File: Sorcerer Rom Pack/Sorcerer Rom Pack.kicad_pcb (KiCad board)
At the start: 2 copper layers, 119.4 x 73.3 mm, 86 parts, among them J1 ROMRD15, J10 A11, J11 A13, J12 A12, J13 A, J14 A, J15 A, J16 A, J17 A, J18 C, J19 B, J2 A14, J20 A, J21 A, J22 A, J23 A, J24 A, J25 A, J26 A, J27 A, J28 Sorcerer Cart Slot, J29 0 ENABLE, J3 ROMRD15, J30 1 ENABLE, J31 4 ENABLE, J32 5 ENABLE, J33 1 PROM, J34 2 PROM, J35 A, J36 A, J37 A, J38 A, J39 A, J4 A12, J40 A, J41 A, J42 A, J43 A, J44 A, J45 A, J46 A, J47 A, J48 A, J49 A, J5 Conn_01x01, J50 A, J51 A, J52 A, J53 A, J54 A, J55 A, J56 A, J57 A, J58 A, J59 A, J6 Conn_01x01, J60 A, J61 A, J62 A, J63 A, J64 A, J65 A, J66 A, J67 A, J68 A, J69 RAM cut, J7 A, J8 A14, J9 A10, U1 2716, U2 2716, U3 2716, U4 2716, U5 74LS11, U6 74LS138

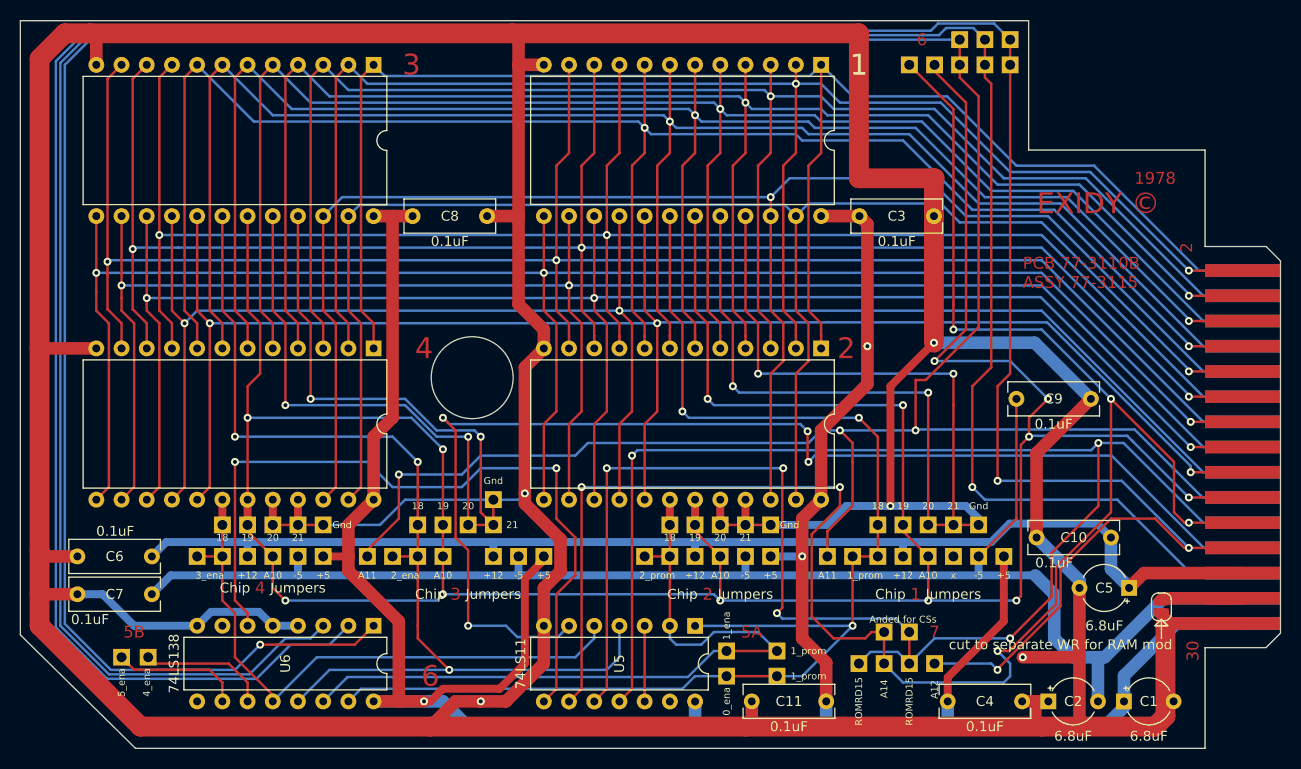
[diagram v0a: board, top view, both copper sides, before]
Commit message: many tweaks and experimental silk
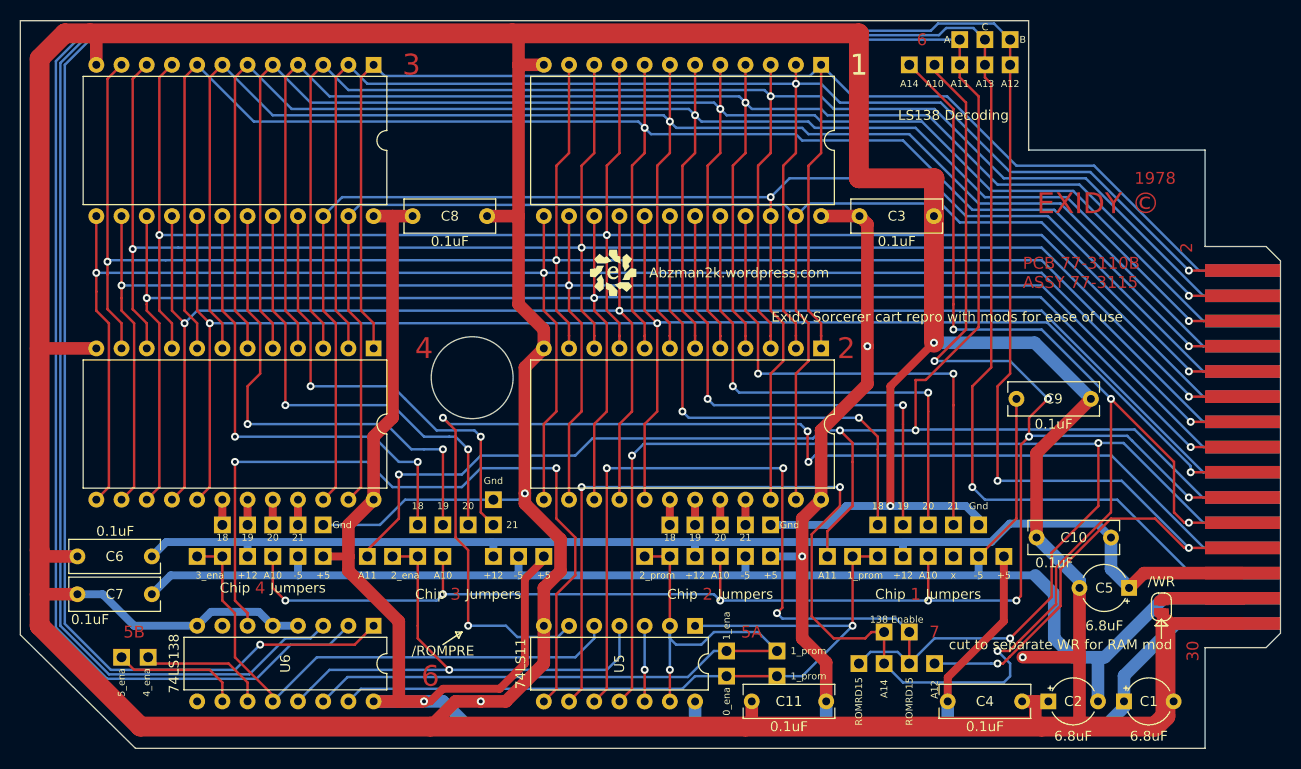
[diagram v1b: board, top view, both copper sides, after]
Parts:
- added G***: LOGO, Evan's misc parts:Evan Logo, F.Cu at (129.5, 95.9)
- added G***: LOGO, Evan's misc parts:OSHW gear, B.Cu at (183.5, 107.3)
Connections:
- J16 pad 1: 30 -> Net-(J16-Pad1)
- J21 pad 1: 30 -> Net-(J21-Pad1)
- J23 pad 1: 20 -> Net-(J23-Pad1)
- J25 pad 1: Net-(J24-Pad1) -> Net-(J25-Pad1)
- J30 pad 1: Net-(J34-Pad1) -> Net-(J30-Pad1)
- J34 pad 1: Net-(J34-Pad1) -> Net-(J30-Pad1)
- J38 pad 1: 30 -> Net-(J38-Pad1)
- J40 pad 1: 30 -> Net-(J40-Pad1)
- J42 pad 1: 20 -> Net-(J42-Pad1)
- J43 pad 1: Net-(J34-Pad1) -> Net-(J30-Pad1)
- J44 pad 1: Net-(J34-Pad1) -> Net-(J44-Pad1)
- J45 pad 1: Net-(J34-Pad1) -> Net-(J30-Pad1)
- J49 pad 1: 30 -> Net-(J49-Pad1)
- J51 pad 1: 30 -> Net-(J51-Pad1)
- J53 pad 1: 20 -> Net-(J53-Pad1)
- J55 pad 1: Net-(J54-Pad1) -> Net-(J55-Pad1)
- J61 pad 1: 30 -> Net-(J61-Pad1)
- J63 pad 1: 30 -> Net-(J63-Pad1)
- J65 pad 1: 20 -> Net-(J65-Pad1)
- J67 pad 1: Net-(J66-Pad1) -> Net-(J67-Pad1)
- U1 pad 18: Net-(J24-Pad1) -> Net-(J25-Pad1)
- U1 pad 19: 20 -> Net-(J23-Pad1)
- U1 pad 20: 30 -> Net-(J21-Pad1)
- U1 pad 21: 30 -> Net-(J16-Pad1)
- U2 pad 18: Net-(J34-Pad1) -> Net-(J44-Pad1)
- U2 pad 19: 20 -> Net-(J42-Pad1)
- U2 pad 20: 30 -> Net-(J40-Pad1)
- U2 pad 21: 30 -> Net-(J38-Pad1)
- U3 pad 18: Net-(J54-Pad1) -> Net-(J55-Pad1)
- U3 pad 19: 20 -> Net-(J53-Pad1)
- U3 pad 20: 30 -> Net-(J51-Pad1)
- U3 pad 21: 30 -> Net-(J49-Pad1)
- U4 pad 18: Net-(J66-Pad1) -> Net-(J67-Pad1)
- U4 pad 19: 20 -> Net-(J65-Pad1)
- U4 pad 20: 30 -> Net-(J63-Pad1)
- U4 pad 21: 30 -> Net-(J61-Pad1)
- U5 pad 13: Net-(J34-Pad1) -> Net-(J30-Pad1)
- U5 pad 2: Net-(J34-Pad1) -> Net-(J30-Pad1)
- U6 pad 14: Net-(J34-Pad1) -> Net-(J30-Pad1)
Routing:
- net 30: track 804.7 -> 576.6 mm, vias 13 -> 5
- net 20: track 313.3 -> 183.1 mm, vias 13 -> 9
- net Net-(J30-Pad1): track 0.00 -> 78.6 mm, vias 0 -> 1
- net Net-(J34-Pad1): track 76.7 -> 0.00 mm
- net Net-(J24-Pad1): track 132.4 -> 79.4 mm, vias 3 -> 1
- net Net-(J54-Pad1): track 104.4 -> 52.7 mm, vias 3 -> 1
- net Net-(J16-Pad1): track 0.00 -> 51.3 mm, vias 0 -> 2
- net Net-(J23-Pad1): track 0.00 -> 51.0 mm, vias 0 -> 2
- net Net-(J21-Pad1): track 0.00 -> 51.0 mm, vias 0 -> 2
- net Net-(J53-Pad1): track 0.00 -> 50.4 mm, vias 0 -> 2
- net Net-(J25-Pad1): track 0.00 -> 49.8 mm, vias 0 -> 2
- net Net-(J55-Pad1): track 0.00 -> 48.6 mm, vias 0 -> 2
- net Net-(J51-Pad1): track 0.00 -> 47.5 mm, vias 0 -> 2
- net Net-(J49-Pad1): track 0.00 -> 46.3 mm, vias 0 -> 2
- net Net-(J66-Pad1): track 61.2 -> 55.5 mm
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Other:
- board text added: "/ROMPRE"
- board text added: "/WR"
- board text added: "138 Enable"
- board text added: "138 Enable jumpers set the starting address A14/ROMRD15 = C000 (use for 8K PAC) A13/ROMRD15 = A000 (use for 16K PAC) A12/ROMRD15 = 9000 ROMRD15 x2 = 8000"
- board text added: "16K ROM PAC 4K ROMS A - A12 B - A13 C - A14"
- board text added: "16K ROM PAC 8K ROMS A - Gnd B - A13 C - A14 Chips 1 and 3"
- board text added: "1K ROM PAC 1K ROMS A - Gnd B - Gnd C - Gnd Chip 1"
- board text added: "2316: 18 - +5 19 - A10 20 - /CS 21 - /CS"
- board text added: "2332: 18 - A11 19 - A10 20 - /CS 21 - +5v"
- board text added: "2364: 18 - A11 19 - A10 20 - /CS 21 - A12"
- board text added: "2K ROM PAC 1K ROMS A - Gnd B - A10 C - A11 Chips 1 and 3"
- board text added: "2K ROM PAC 2K ROMS A - Gnd B - Gnd C - Gnd Chip 1"
- board text added: "4K ROM PAC 1K ROMS A - A10 B - A11 C - A12"
- board text added: "4K ROM PAC 2K ROMS A - Gnd B - A11 C - A12 Chips 1 and 3"
- board text added: "4K ROM PAC 4K ROMS A - Gnd B - Gnd C - Gnd Chip 1"
- board text added: "8K ROM PAC 2K ROMS A - A11 B - A12 C - A13"
- board text added: "8K ROM PAC 4K ROMS A - Gnd B - A12 C - A13 Chips 1 and 3"
- board text added: "8K ROM PAC 8K ROMS A - Gnd B - Gnd C - Gnd Chip 1"
- board text added: "A"
- board text added: "A13"
- board text added: "AM9218/factory PROM: 18 - /CS 19 - A10 20 - Gnd 21 - Gnd"
- board text added: "Abzman2k.wordpress.com"
- board text added: "All 4 ROM decodes always disable internal RAM unless you start cutting traces labeled A-F"
- board text added: "B"
- board text added: "C"
- board text added: "D"
- board text added: "E"
- board text added: "Exidy Sorcerer cart repro with mods for ease of use"
- board text added: "F"
- board text added: "G"
- board text added: "LS138 Decoding"
- board text added: "Make sure the 4011 gates that drive pin 23 set it high only when this cart takes precedence over internal RAM"
- board text added: "TMS2716: 18 - /CS 19 - +12 20 - A10 21 - -5"
- board text added: "The 138 decoder address lines choose how big the banks are"
- board text added: "There is a max of 4 chips but 6 banks are broken out so you can offset your memory locations by 1 or 2 banks"
- board text added: "You can mix and match RAM and ROM chips"
- board text added: "if not using +12v, omit C5, C6 and C10"
- board text added: "if not using -5v, omit C2, C7 and C9"
- board text removed: "Anded for CSs"
- board text removed: "To reuse pin 26 as data and not +12v remove C5, C6 and C10"
- board text removed: "To reuse pin 27 as data and not -5v remove C2, C7 and C9"

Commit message: removed temp files, added gitignore, fixed silk on rom pac board
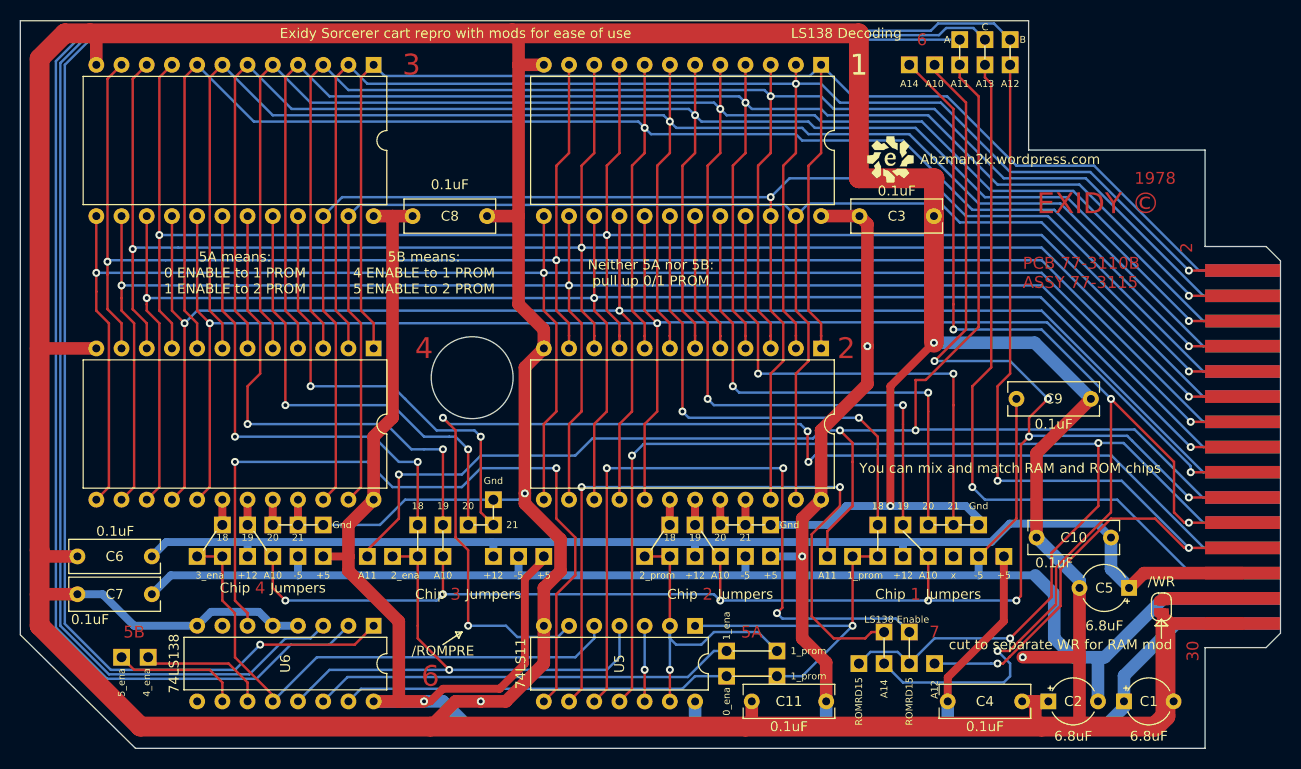
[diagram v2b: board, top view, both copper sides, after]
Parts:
- moved G*** 30.2 mm to (157.5, 84.5)
- moved G*** 28.5 mm to (165.7, 129.5)
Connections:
- J17 pad 1: 19 -> Net-(J17-Pad1)
- J18 pad 1: 25 -> Net-(J18-Pad1)
- J19 pad 1: 24 -> Net-(J19-Pad1)
- J29 pad 1: Net-(J24-Pad1) -> Net-(J29-Pad1)
- J34 pad 1: Net-(J30-Pad1) -> Net-(J34-Pad1)
- J43 pad 1: Net-(J30-Pad1) -> Net-(J34-Pad1)
- J45 pad 1: Net-(J30-Pad1) -> Net-(J34-Pad1)
- J5 pad 1: 22 -> Net-(J5-Pad1)
- J6 pad 1: 21 -> Net-(J6-Pad1)
- U5 pad 10: 21 -> Net-(J6-Pad1)
- U5 pad 13: Net-(J30-Pad1) -> Net-(J34-Pad1)
- U5 pad 2: Net-(J30-Pad1) -> Net-(J34-Pad1)
- U5 pad 9: 22 -> Net-(J5-Pad1)
- U6 pad 1: 19 -> Net-(J17-Pad1)
- U6 pad 15: Net-(J24-Pad1) -> Net-(J29-Pad1)
- U6 pad 2: 24 -> Net-(J19-Pad1)
- U6 pad 3: 25 -> Net-(J18-Pad1)
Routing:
- net 24: track 296.9 -> 105.0 mm
- net Net-(J19-Pad1): track 0.00 -> 189.3 mm
- net 19: track 339.4 -> 154.4 mm, vias 4 -> 3
- net 25: track 259.3 -> 74.4 mm
- net Net-(J17-Pad1): track 0.00 -> 182.4 mm, vias 0 -> 1
- net Net-(J18-Pad1): track 0.00 -> 182.3 mm
- net 22: track 190.4 -> 116.3 mm, vias 6 -> 4
- net 21: track 205.2 -> 131.3 mm, vias 6 -> 3
- net Net-(J5-Pad1): track 0.00 -> 70.8 mm, vias 0 -> 2
- net Net-(J6-Pad1): track 0.00 -> 70.7 mm, vias 0 -> 3
- net Net-(J24-Pad1): track 79.4 -> 35.1 mm
- net Net-(J29-Pad1): track 0.00 -> 39.2 mm
- net Net-(J30-Pad1): track 78.6 -> 42.7 mm, vias 1 -> 0
- net Net-(J34-Pad1): track 0.00 -> 30.8 mm, vias 0 -> 1
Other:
- board text added: "16K ROM PAC, 4K ROMS 5B 6 - A to A12, B to A13, C to A14 7 - ROMRD15 and ROMRD15 A000-AFFF - ROM 3 B000-BFFF - ROM 4 C000-CFFF - ROM 1 D000-DFFF - ROM 2"
- board text added: "4K ROM PAC, 1K ROMS 5A 6 - A to A10, B to A11, C to A13 7 - A12 and A14 D000-D3FF - ROM 1 D400-D7FF - ROM 2 D800-DBFF - ROM 3 DC00-DFFF - ROM 4"
- board text added: "4K ROM PAC, 2K ROMS 5A 6 - A to A12, B to A11, C to A13 7 - A12 and A14 D000-D7FF - ROM 2 D800-DFFF - ROM 4"
- board text added: "4K ROM PAC, 2K ROMS 6 - A to A11, B to A12, C to A13 7 - ROMRD15 and A14 D000-D7FF - ROM 3 D800-DFFF - ROM 4"
- board text added: "4K ROM PAC, 4K ROM 6 - A to A13, B to A12, C to A13 7 - ROMRD15 and A14 D000-DFFF - ROM 3"
- board text added: "5A means: 0 ENABLE to 1 PROM 1 ENABLE to 2 PROM"
- board text added: "5B means: 4 ENABLE to 1 PROM 5 ENABLE to 2 PROM"
- board text added: "8K ROM PAC, 2K ROMS 5A 6 - A to A11, B to A12, C to A13 7 - ROMRD15 and A14 C000-C7FF - ROM 1 C800-CFFF - ROM 2 D000-D7FF - ROM 3 D800-DFFF - ROM 4"
- board text added: "8K ROM PAC, 4K ROMS 5A 6 - A to A13, B to A12, C to A13 7 - ROMRD15 and A14 C000-CFFF - ROM 1 D000-DFFF - ROM 3"
- board text added: "LS138 Enable"
- board text added: "Neither 5A nor 5B: pull up 0/1 PROM"
- board text removed: "138 Enable"
- board text removed: "138 Enable jumpers set the starting address A14/ROMRD15 = C000 (use for 8K PAC) A13/ROMRD15 = A000 (use for 16K PAC) A12/ROMRD15 = 9000 ROMRD15 x2 = 8000"
- board text removed: "16K ROM PAC 4K ROMS A - A12 B - A13 C - A14"
- board text removed: "16K ROM PAC 8K ROMS A - Gnd B - A13 C - A14 Chips 1 and 3"
- board text removed: "1K ROM PAC 1K ROMS A - Gnd B - Gnd C - Gnd Chip 1"
- board text removed: "2316: 18 - +5 19 - A10 20 - /CS 21 - /CS"
- board text removed: "2332: 18 - A11 19 - A10 20 - /CS 21 - +5v"
- board text removed: "2364: 18 - A11 19 - A10 20 - /CS 21 - A12"
- board text removed: "2K ROM PAC 1K ROMS A - Gnd B - A10 C - A11 Chips 1 and 3"
- board text removed: "2K ROM PAC 2K ROMS A - Gnd B - Gnd C - Gnd Chip 1"
- board text removed: "4K ROM PAC 1K ROMS A - A10 B - A11 C - A12"
- board text removed: "4K ROM PAC 2K ROMS A - Gnd B - A11 C - A12 Chips 1 and 3"
- board text removed: "4K ROM PAC 4K ROMS A - Gnd B - Gnd C - Gnd Chip 1"
- board text removed: "8K ROM PAC 2K ROMS A - A11 B - A12 C - A13"
- board text removed: "8K ROM PAC 4K ROMS A - Gnd B - A12 C - A13 Chips 1 and 3"
- board text removed: "8K ROM PAC 8K ROMS A - Gnd B - Gnd C - Gnd Chip 1"
- board text removed: "All 4 ROM decodes always disable internal RAM unless you start cutting traces labeled A-F"
- board text removed: "D"
- board text removed: "E"
- board text removed: "F"
- board text removed: "G"
- board text removed: "Make sure the 4011 gates that drive pin 23 set it high only when this cart takes precedence over internal RAM"
- board text removed: "The 138 decoder address lines choose how big the banks are"
- board text removed: "There is a max of 4 chips but 6 banks are broken out so you can offset your memory locations by 1 or 2 banks"
